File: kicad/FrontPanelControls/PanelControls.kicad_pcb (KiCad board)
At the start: 2 copper layers, 106 x 37.8 mm, 39 parts, among them J1 Conn_02x04_Odd_Even, SW5 ADJ, U1 PCF8591, U2 PCF8574, U3 WS2812D, U4 WS2812D, U5 WS2812D, U6 WS2812D, U7 WS2812D, U8 WS2812D

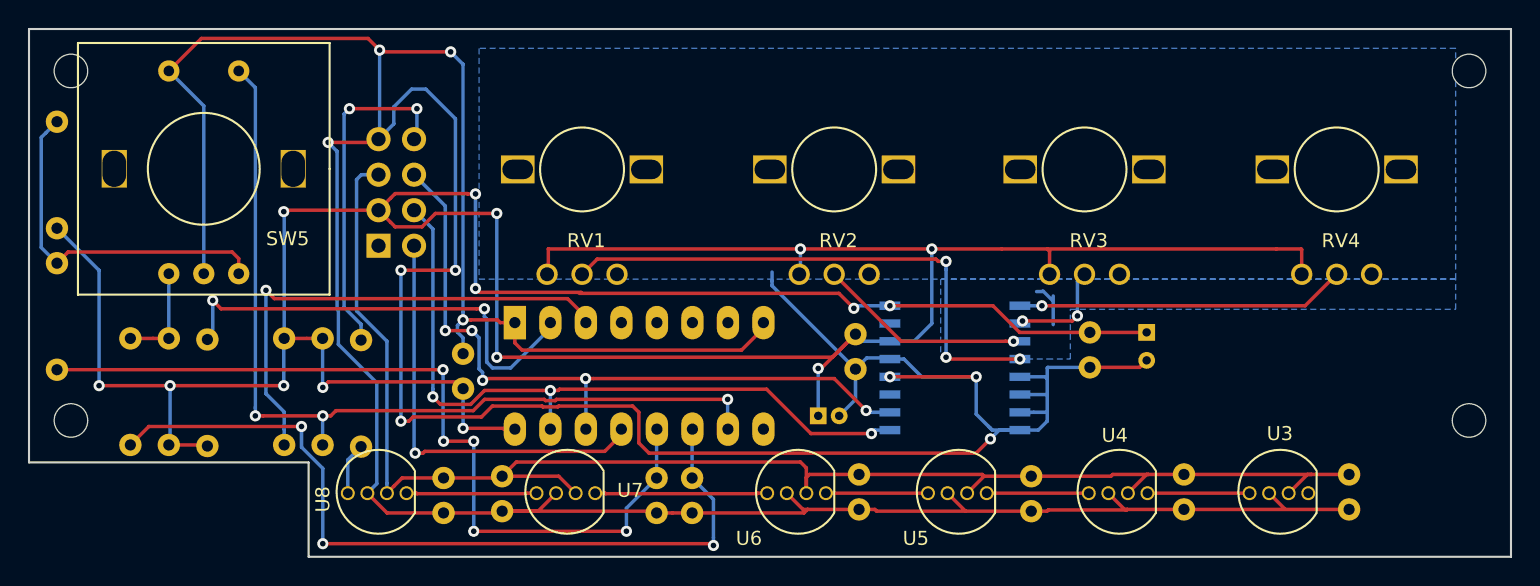
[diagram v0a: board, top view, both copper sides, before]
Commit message: New front panel (#86)
v0.2 of front panel. light up led buttons, new adc, new i/o expander
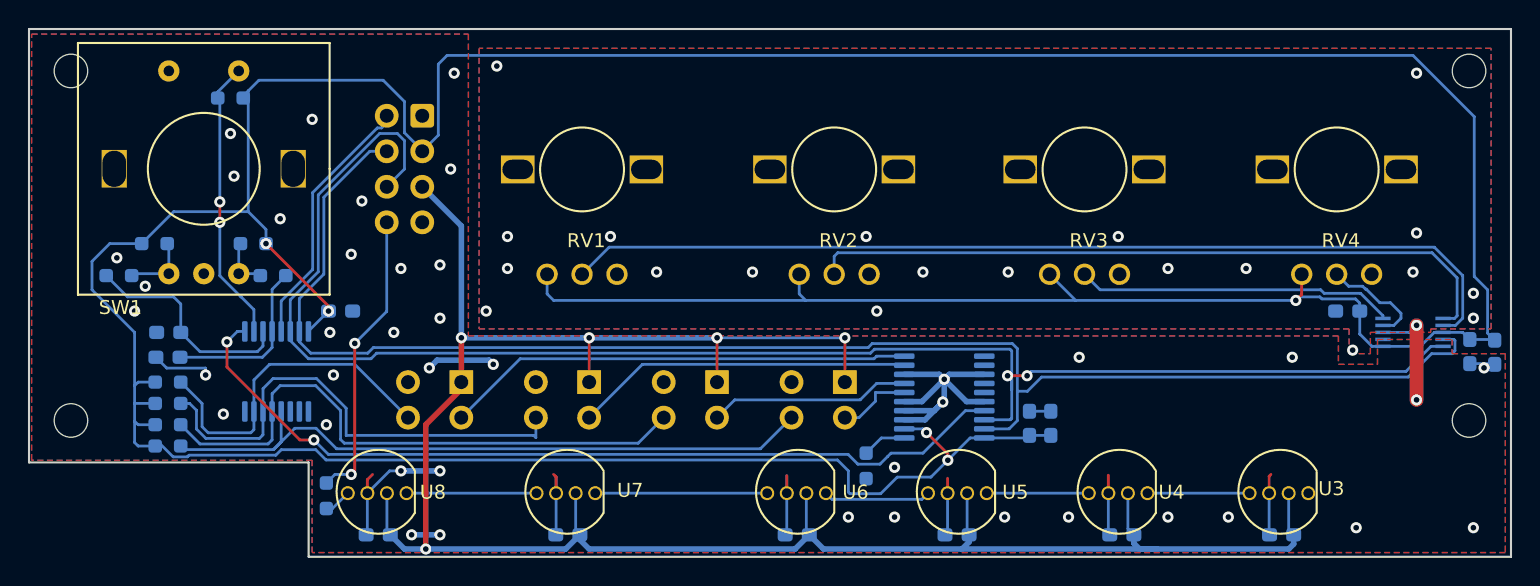
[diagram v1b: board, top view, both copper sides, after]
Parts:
- removed C18, C3: 100nF, Capacitor_THT:C_Disc_D3.0mm_W2.0mm_P2.50mm
- removed R19, R20, R25, R26, R28: 10K, Resistor_THT:R_Axial_DIN0207_L6.3mm_D2.5mm_P7.62mm_Horizontal
- removed R29: 100R, Resistor_THT:R_Axial_DIN0207_L6.3mm_D2.5mm_P7.62mm_Horizontal
- removed SW5: ADJ, ProjLib:BOURNS PEC11L-4125F-S0020
- added C13: 100nF, Capacitor_SMD:C_0603_1608Metric_Pad1.08x0.95mm_HandSolder, B.Cu at (113.3, 138.2)
- added C14: 100nF, Capacitor_SMD:C_0603_1608Metric_Pad1.08x0.95mm_HandSolder, B.Cu at (100.9, 141.5)
- added C15: 100nF, Capacitor_SMD:C_0603_1608Metric_Pad1.08x0.95mm_HandSolder, B.Cu at (101.0, 139.7)
- added J2: BUTTON_B, Library:ButtonConnector, B.Cu at (137.9, 144.5)
- added J3: BUTTON_C, Library:ButtonConnector, B.Cu at (128.8, 144.5)
- added J4: BUTTON_D, Library:ButtonConnector, B.Cu at (119.6, 144.5)
- added J5: Conn_02x04_Odd_Even, Connector_IDC:IDC-Header_2x04_P2.54mm_Vertical, B.Cu at (119.1, 124.2)
- added R1: 100R, Resistor_SMD:R_0603_1608Metric_Pad0.98x0.95mm_HandSolder, B.Cu at (112.3, 151.4)
- added R11: 10K, Resistor_SMD:R_0603_1608Metric_Pad0.98x0.95mm_HandSolder, B.Cu at (105.4, 122.9)
- added R2: 10K, Resistor_SMD:R_0603_1608Metric_Pad0.98x0.95mm_HandSolder, B.Cu at (100.9, 147.8)
- added R3: 10K, Resistor_SMD:R_0603_1608Metric_Pad0.98x0.95mm_HandSolder, B.Cu at (100.9, 146.3)
- added R4: 10K, Resistor_SMD:R_0603_1608Metric_Pad0.98x0.95mm_HandSolder, B.Cu at (100.9, 144.8)
- added R5: 10K, Resistor_SMD:R_0603_1608Metric_Pad0.98x0.95mm_HandSolder, B.Cu at (100.9, 143.3)
- added R6: 1K, Resistor_SMD:R_0603_1608Metric_Pad0.98x0.95mm_HandSolder, B.Cu at (150.9, 149.2)
- added R7: 10K, Resistor_SMD:R_0603_1608Metric_Pad0.98x0.95mm_HandSolder, B.Cu at (107.0, 133.3)
- added R8: 10K, Resistor_SMD:R_0603_1608Metric_Pad0.98x0.95mm_HandSolder, B.Cu at (100.0, 133.3)
- added SW1: ADJ, ProjLib:BOURNS PEC11L-4125F-S0020, F.Cu at (103.5, 128.0)
- added U9: TLC59108IPWR, Package_SO:TSSOP-20_4.4x6.5mm_P0.65mm, B.Cu at (156.5, 144.3)
- C1, C10, C11, C5, C6, C7, C8, C9: footprint Capacitor_THT:C_Disc_D3.0mm_W2.0mm_P2.50mm -> Capacitor_SMD:C_0603_1608Metric_Pad1.08x0.95mm_HandSolder
- C12: value 100nF -> 10uF; footprint Capacitor_THT:C_Disc_D3.0mm_W2.0mm_P2.50mm -> Capacitor_SMD:C_0603_1608Metric_Pad1.08x0.95mm_HandSolder
- C2: footprint Capacitor_THT:CP_Radial_D4.0mm_P2.00mm -> Capacitor_SMD:C_0603_1608Metric_Pad1.08x0.95mm_HandSolder
- C4: value 10uF -> 100nF; footprint Capacitor_THT:CP_Radial_D4.0mm_P1.50mm -> Capacitor_SMD:C_0603_1608Metric_Pad1.08x0.95mm_HandSolder
- J1: value Conn_02x04_Odd_Even -> BUTTON_A; footprint Connector_IDC:IDC-Header_2x04_P2.54mm_Vertical -> Library:ButtonConnector
- R10, R9: footprint Resistor_THT:R_Axial_DIN0207_L6.3mm_D2.5mm_P7.62mm_Horizontal -> Resistor_SMD:R_0603_1608Metric_Pad0.98x0.95mm_HandSolder
- U1: value PCF8591 -> ADS1115IDGS; footprint Package_SO:SOIC-16W_7.5x10.3mm_P1.27mm -> Package_SO:TSSOP-10_3x3mm_P0.5mm
- U2: value PCF8574 -> TCA9534; footprint Package_DIP:DIP-16_W7.62mm_LongPads -> Package_SO:TSSOP-16_4.4x5mm_P0.65mm
- moved C5 60.1 mm to (180.6, 154.2), turned to 180 degrees
- moved C6 44.5 mm to (169.2, 154.2), turned to 180 degrees
- moved C12 42.3 mm to (164.1, 146.2), turned to 90 degrees
- moved C4 38.6 mm to (185.3, 138.2), turned to 180 degrees
- moved J1 33.0 mm to (147.1, 144.5), turned to 180 degrees
- moved U1 32.9 mm to (190.0, 139.7), turned to 0 degrees
- moved C1 27.2 mm to (194.1, 141.1)
- moved C2 24.9 mm to (195.8, 141.1)
- moved C10 22.8 mm to (116.0, 154.2), turned to 180 degrees
- moved U2 17.4 mm to (108.7, 142.5), turned to 90 degrees
- moved R9 15.8 mm to (108.5, 135.6), turned to 180 degrees
- moved R10 12.6 mm to (97.4, 135.6), turned to 180 degrees
- moved C11 11.6 mm to (162.6, 146.2), turned to 90 degrees
- moved C9 7.54 mm to (129.5, 154.2), turned to 180 degrees
- moved C7 6.76 mm to (157.4, 154.2), turned to 180 degrees
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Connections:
- C10 pad 1: ROT5-A -> +5v
- C11 pad 1: +5v -> +3v3
- C12 pad 1: GND -> +3v3
- C12 pad 2: +3v3 -> GND
- C9 pad 1: ROT5-B -> +5v
- J1 pad 1: (no net) -> +5v
- J1 pad 2: INT2 -> GND
- J1 pad 3: +3v3 -> Net-(J1-Pad3)
- J1 pad 4: SDA -> Net-(J1-Pad4)
- R10 pad 1: +3v3 -> Net-(R10-Pad1)
- R10 pad 2: Net-(R10-Pad2) -> ROT5-A
- R9 pad 1: +3v3 -> ROT5-B
- U1 pad 1: Net-(RV4-Pad2) -> +3v3
- U1 pad 2: Net-(RV3-Pad2) -> unconnected-(U1-Pad2)
- U1 pad 3: Net-(RV2-Pad2) -> GND
- U1 pad 4: Net-(RV1-Pad2) -> Net-(RV4-Pad2)
- U1 pad 5: GND -> Net-(RV3-Pad2)
- U1 pad 6: GND -> Net-(RV2-Pad2)
- U1 pad 7: GND -> Net-(RV1-Pad2)
- U1 pad 8: GND -> +3v3
- U2 pad 2: Net-(R26-Pad1) -> GND
- U2 pad 3: Net-(R28-Pad1) -> GND
- U2 pad 4: (no net) -> Net-(J1-Pad4)
- U2 pad 5: (no net) -> Net-(J2-Pad4)
- U2 pad 6: (no net) -> Net-(J3-Pad4)
- U2 pad 7: (no net) -> Net-(J4-Pad4)
- U2 pad 9: (no net) -> RESET
- U3 pad 1: (no net) -> unconnected-(U3-Pad1)
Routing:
- net GND: track 345.5 -> 78.4 mm, vias 10 -> 62
- net SCL: track 51.7 -> 115.7 mm, vias 5 -> 2
- net RESET: track 0.00 -> 62.0 mm, vias 0 -> 2
- net SDA: track 51.5 -> 110.9 mm, vias 3 -> 0
- net +3v3: track 266.0 -> 322.3 mm, vias 15 -> 5
- net Net-(J1-Pad4): track 0.00 -> 48.9 mm
- net ROT5-B: track 60.5 -> 12.4 mm, vias 5 -> 0
- net ROT5-BUT: track 63.7 -> 20.3 mm, vias 3 -> 2
- net ROT5-A: track 58.8 -> 15.9 mm, vias 3 -> 0
- net Net-(J2-Pad4): track 0.00 -> 42.5 mm
- net +5v: track 109.8 -> 151.3 mm, vias 0 -> 5
- net Net-(R28-Pad1): track 35.7 -> 0.00 mm, vias 1 -> 0
- net Net-(J3-Pad4): track 0.00 -> 35.2 mm
- net Net-(RV2-Pad2): track 15.3 -> 50.5 mm, vias 1 -> 0
- net Net-(J4-Pad3): track 0.00 -> 33.5 mm
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- added copper zone on F.Cu, net GND
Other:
- net class Default removed
- board text added: "ZC95-FrontPanel-Analog(back) v0.2"
- board text removed: "ZC95-FrontPanel-Analog(back) v0.1"
